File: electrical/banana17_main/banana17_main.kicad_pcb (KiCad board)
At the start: 2 copper layers, 100 x 100 mm, 66 parts, among them J1 USB_C_Receptacle_USB2.0_16P, SW1 SW, SW10 SW, SW11 SW, SW12 SW, SW13 SW, SW14 SW, SW15 SW, SW16 SW, SW17 SW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

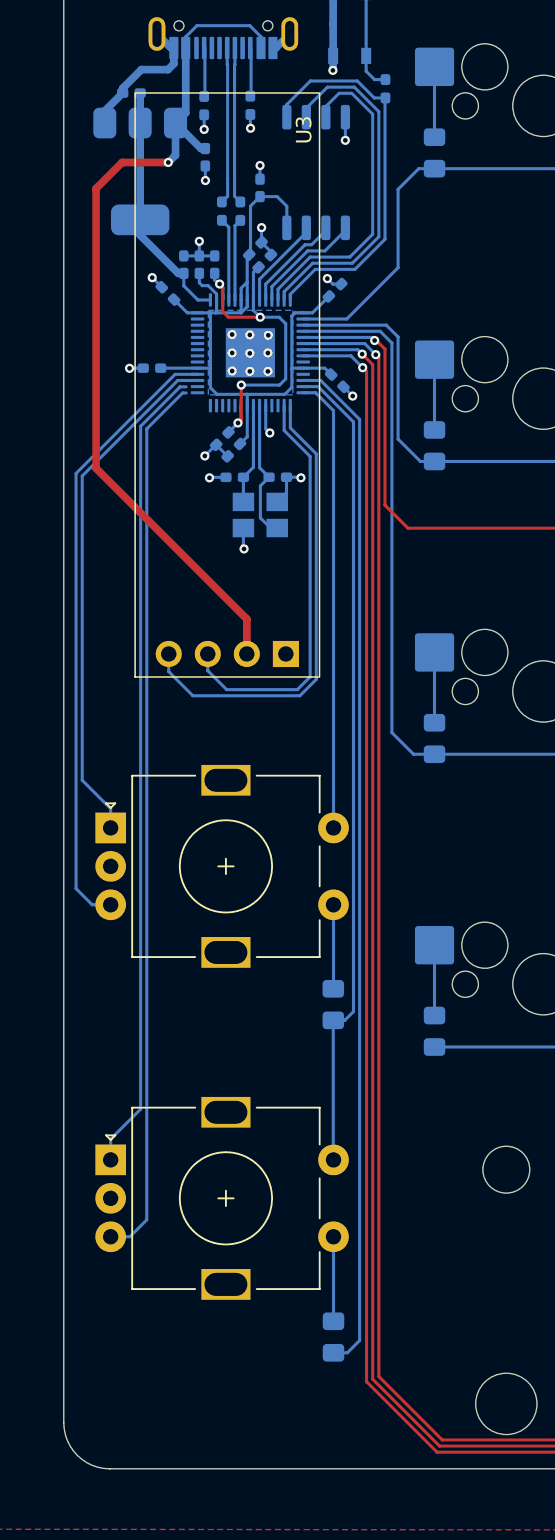
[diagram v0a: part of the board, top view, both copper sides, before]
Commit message: All traces have been drawn. PCB review complete. See description for info.
PCB Review Comments:
1. Should use 4 layers for splitting the 1v1 and 3v3 better and reducing loop from matrix
    - Signal
    - GND
    - Split Plane
    - Signal
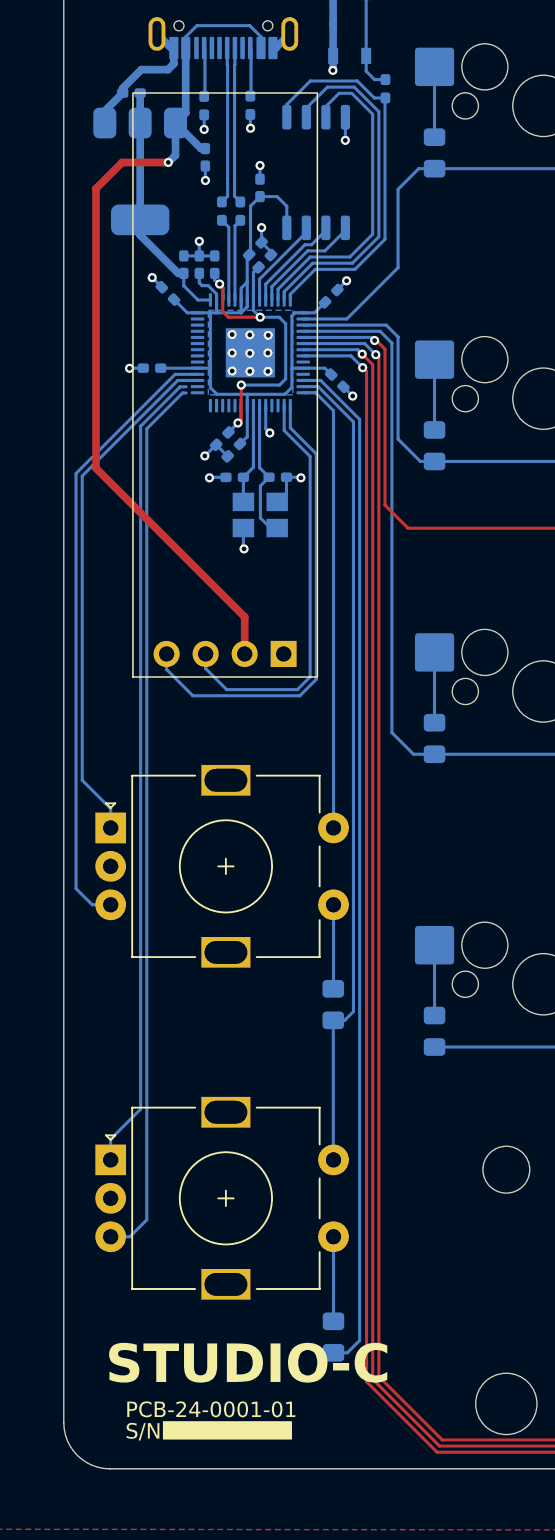
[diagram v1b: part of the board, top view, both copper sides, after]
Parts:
- moved C5 0.46 mm to (112.4, 76.7)
- moved U3 0.14 mm to (105.5, 82.5)
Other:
- board text added: "BOOT"
- board text added: "PCB-24-0001-01"
- board text added: "S/N"
- board text added: "STUDIO-C"

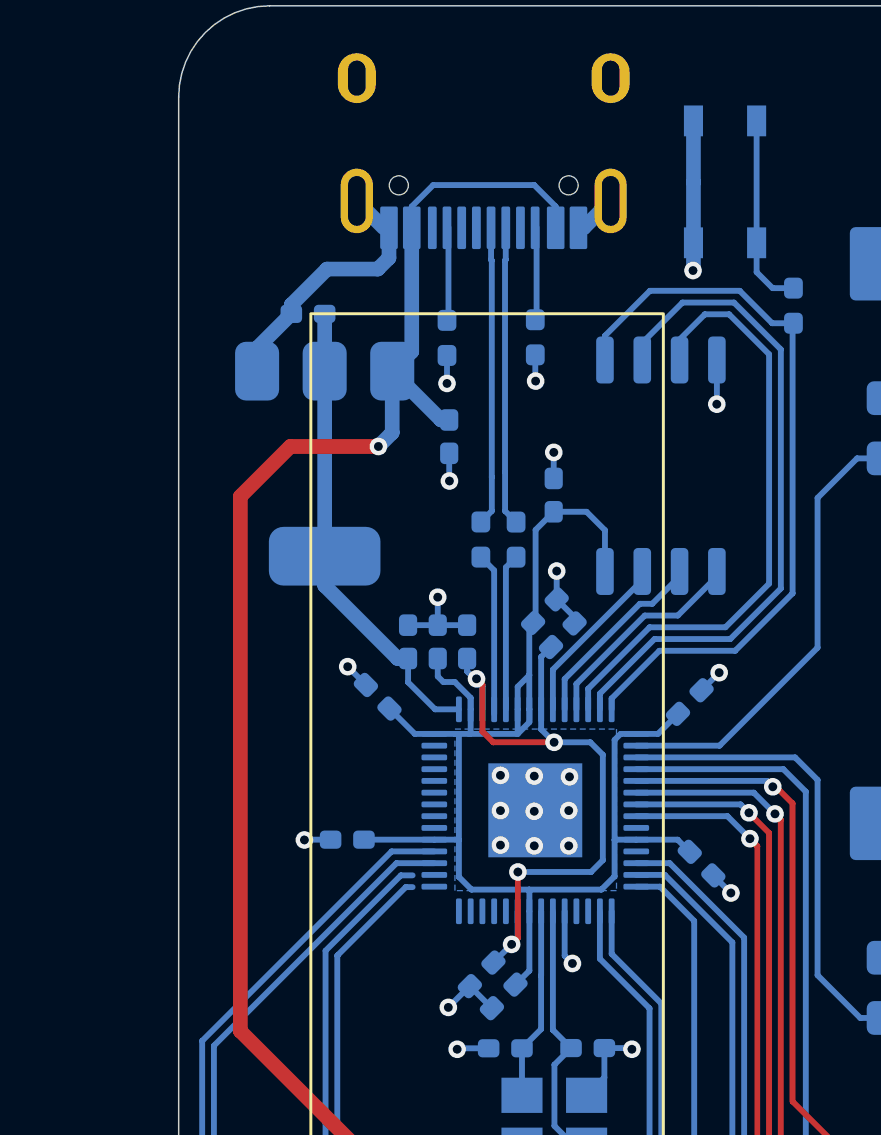
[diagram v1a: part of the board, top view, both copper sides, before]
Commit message: Additional changes to routing from DRC.
Additional changes to routing from DRC.
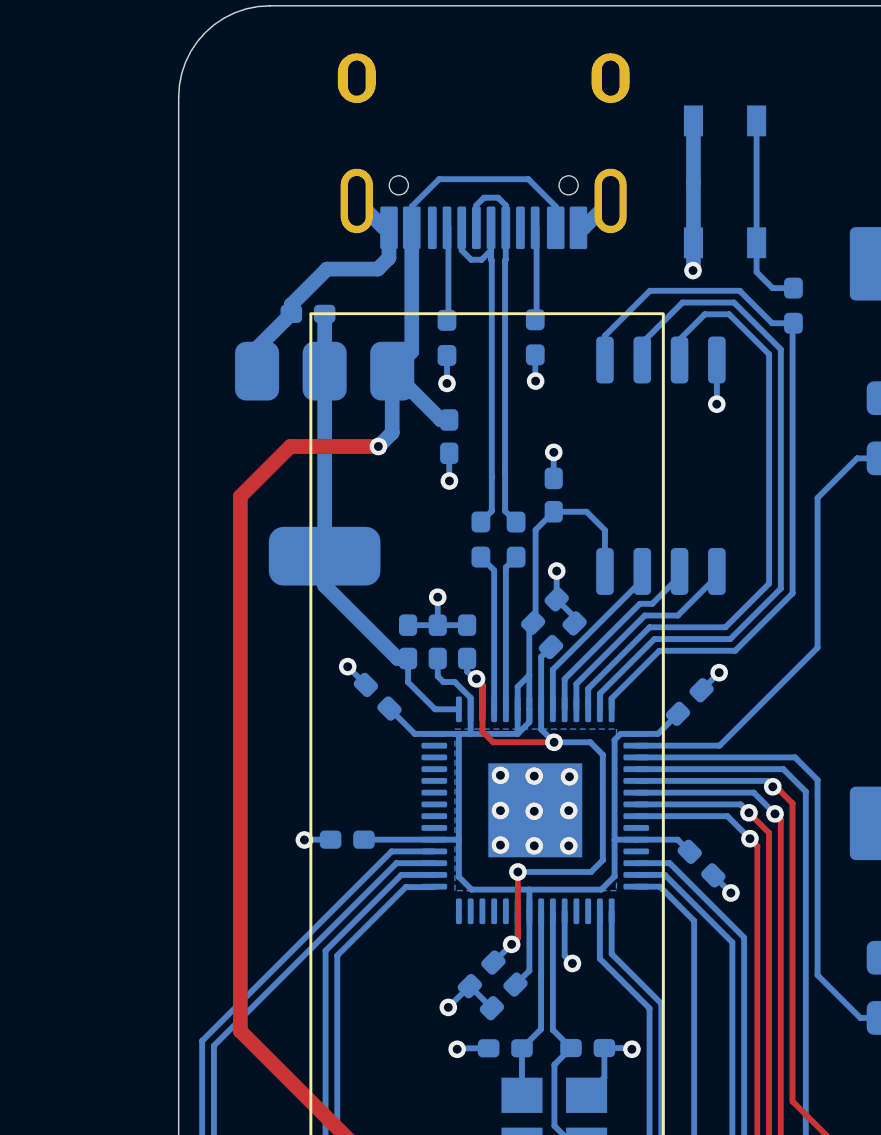
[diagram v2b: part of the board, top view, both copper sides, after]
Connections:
- U1 pad 29: /GPIO18 -> ENC2_B
- U1 pad 30: /GPIO19 -> ENC2_A
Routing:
- net /USB_D-: track 10.2 -> 13.0 mm
- net /USB_D+: track 10.2 -> 12.9 mm
- net ENC2_B: track 57.8 -> 58.5 mm
- net ENC2_A: track 52.6 -> 53.3 mm

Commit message: Ready for production.
Ready for production.
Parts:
- moved R3 1.51 mm to (103.8, 62.8)
- moved R4 1.43 mm to (107.8, 63.0)
- moved R2 1.25 mm to (105.4, 72.4)
- moved R1 1.24 mm to (106.4, 72.4)
- moved C1 0.82 mm to (104.1, 74.3)
- moved C11 0.82 mm to (102.1, 74.3)
- moved C4 0.82 mm to (103.1, 74.3)
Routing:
- net GND: track 38.6 -> 34.2 mm, vias 26 -> 27
- net +3V3: track 64.8 -> 63.1 mm
- net +1V1: track 24.2 -> 25.8 mm
- net /MCU_D+: track 5.54 -> 4.07 mm
- net Net-(J1-CC1): track 3.15 -> 1.80 mm
- net /MCU_D-: track 5.32 -> 4.06 mm
- net /USB_D+: track 12.9 -> 14.1 mm
- net Net-(J1-CC2): track 3.14 -> 2.14 mm
- net COL4: track 250.0 -> 249.5 mm
